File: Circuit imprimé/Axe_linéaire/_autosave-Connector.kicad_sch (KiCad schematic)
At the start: 2 parts, among them J1 Conn_01x14_Shielded

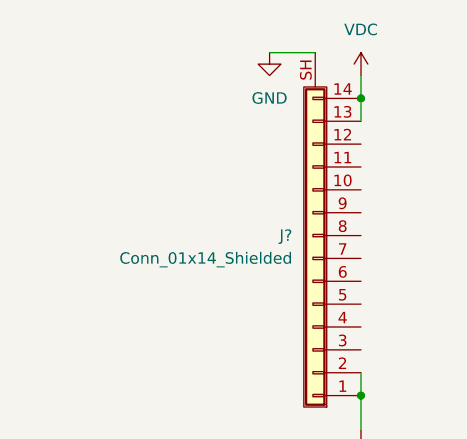
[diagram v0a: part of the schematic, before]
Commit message: Ajout de l'IMU + modèle du photointerrupteur
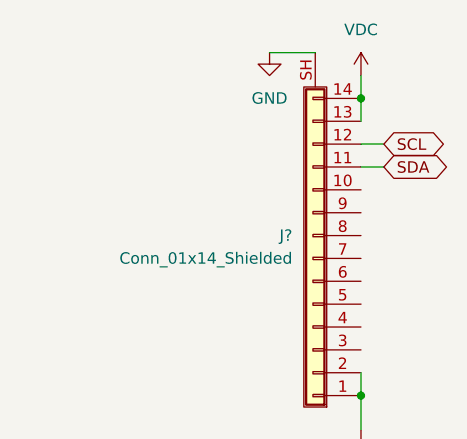
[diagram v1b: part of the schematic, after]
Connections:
- net SDA: now reaches J?.11 (Pin_11)
- net SCL: now reaches J?.12 (Pin_12)
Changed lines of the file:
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@@
+    (stroke (width 0) (type default) (color 0 0 0 0))
+  )
+  (wire (pts (xy 115.57 27.94) (xy 118.11 27.94))
     (stroke (width 0) (type default) (color 0 0 0 0))
   )
@@
   )
   (wire (pts (xy 115.57 17.78) (xy 115.57 20.32))
+    (stroke (width 0) (type default) (color 0 0 0 0))
+  )
+  (wire (pts (xy 115.57 25.4) (xy 118.11 25.4))
     (stroke (width 0) (type default) (color 0 0 0 0))
   )
@@
     )
   )
+  (global_label "SCL" (shape bidirectional) (at 118.11 25.4 0) (fields_autoplaced)
+    (effects (font (size 1.27 1.27)) (justify left))
+    (property "Intersheet References" "${INTERSHEET_REFS}" (id 0) (at 124.0307 25.3206 0)
+      (effects (font (size 1.27 1.27)) (justify left) hide)
+    )
+  )
   (global_label "Motor_A" (shape input) (at 29.21 30.48 0) (fields_autoplaced)
     (effects (font (size 1.27 1.27)) (justify left))
@@
       (effects (font (size 1.27 1.27)) (justify left) hide)
     )
+  )
+  (global_label "SDA" (shape bidirectional) (at 118.11 27.94 0) (fields_autoplaced)
+    (effects (font (size 1.27 1.27)) (justify left))
+    (property "Intersheet References" "${INTERSHEET_REFS}" (id 0) (at 124.0912 27.8606 0)
+      (effects (font (size 1.27 1.27)) (justify left) hide)
+    )
